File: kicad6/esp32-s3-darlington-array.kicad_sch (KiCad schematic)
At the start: 31 parts, among them J1 B5B-XH-A, J2 USB_C_Receptacle_USB2.0, J3 Conn_01x03_Male, J4 Conn_01x08_Male, J5 Conn_01x03_Male, SW1 SW_Push, SW2 SW_Push, U1 ULN2003A, U2 ESP32-S3-WROOM-1, U3 AP2112K/RT9080-3.3

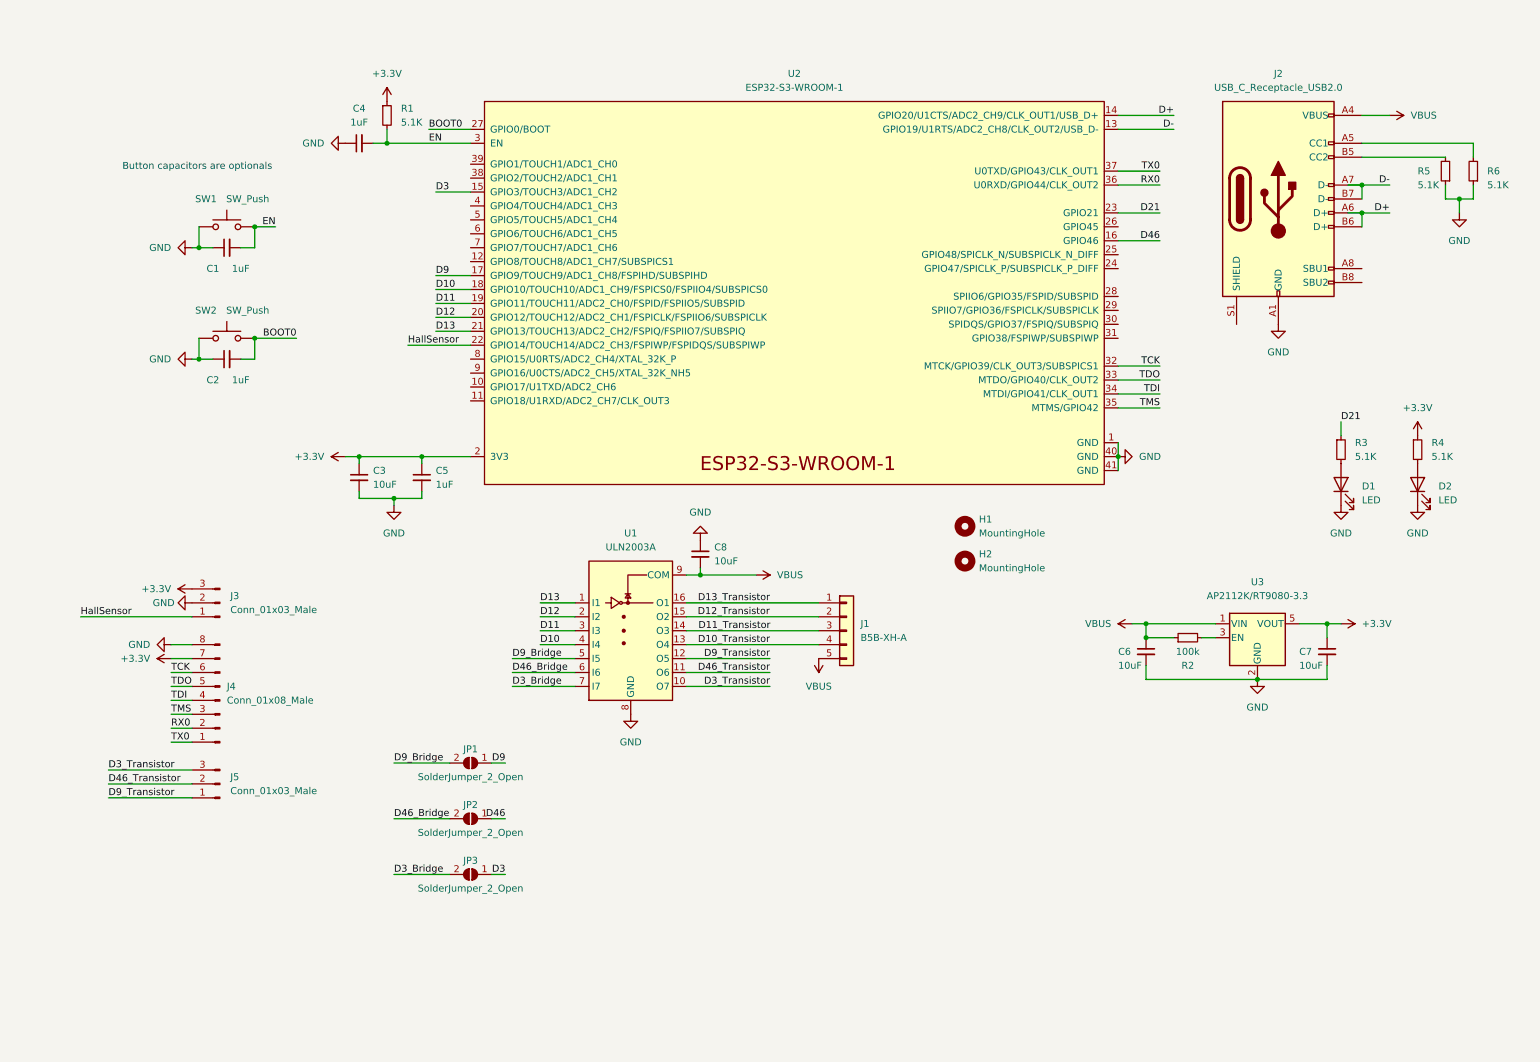
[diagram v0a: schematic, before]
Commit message: Add schematics
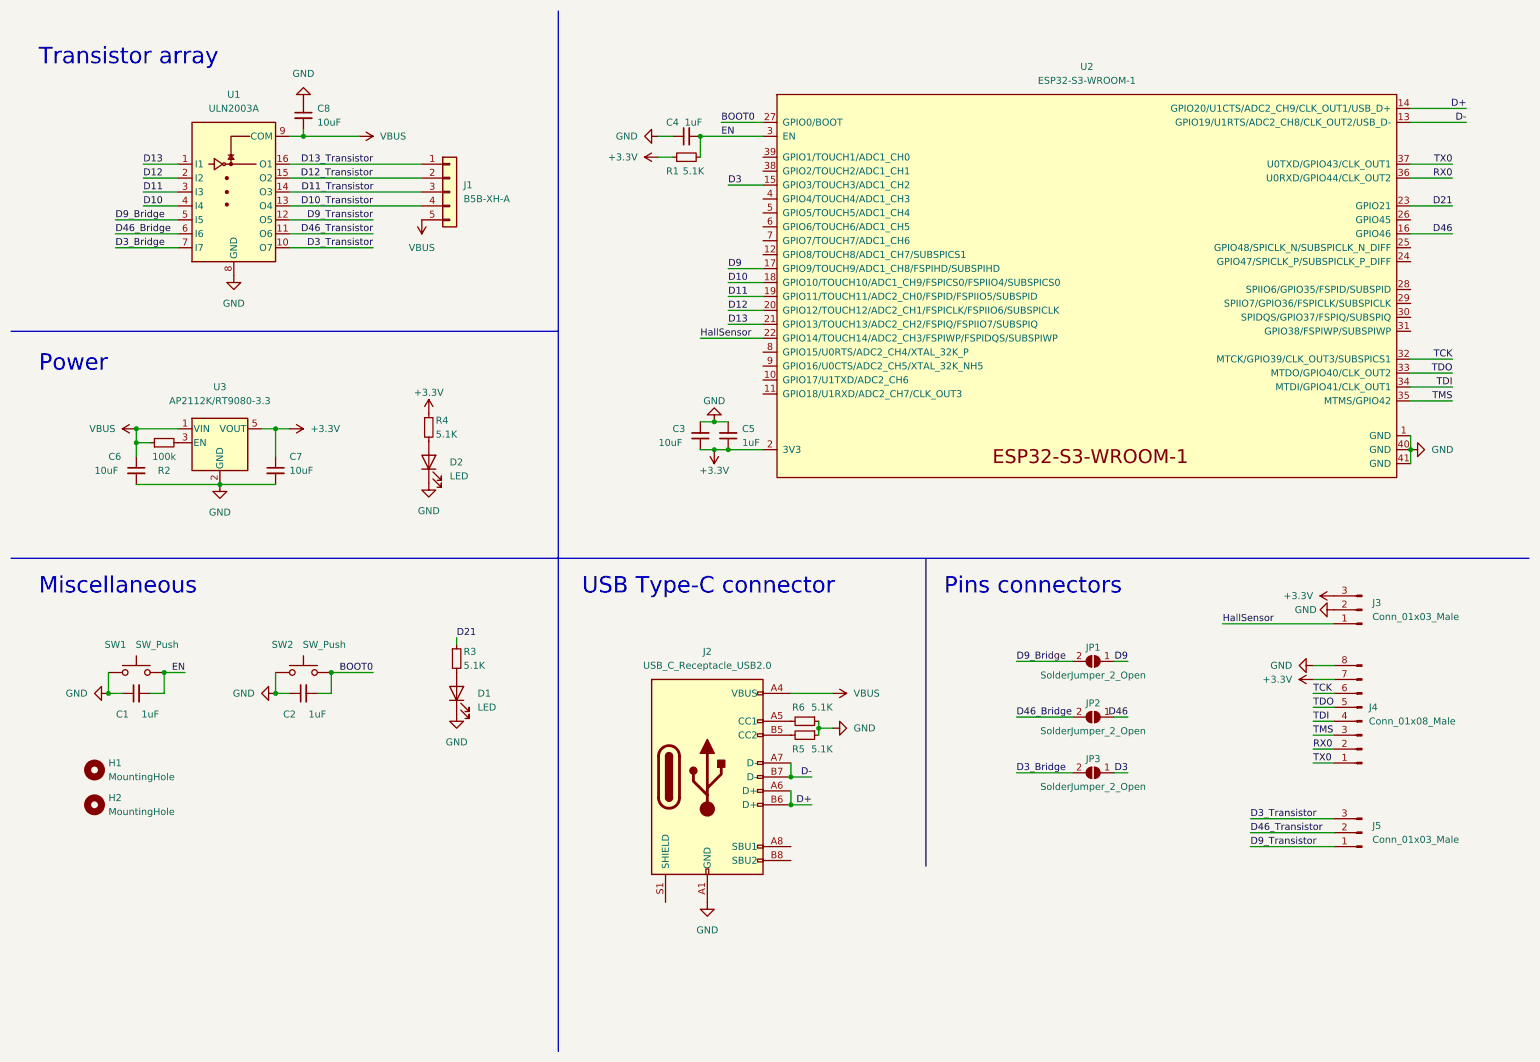
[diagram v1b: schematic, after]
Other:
- note added: "Miscellaneous"
- note added: "Pins connectors"
- note added: "Power"
- note added: "Transistor array"
- note added: "USB Type-C connector"
- note removed: "Button capacitors are optionals"
- title: (none) -> ESP32-S3 with Darlington transistors array
- moved on the sheet: C1, C2, C3, C4, C5, C6, C7, C8, D1, D2, H1, H2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
